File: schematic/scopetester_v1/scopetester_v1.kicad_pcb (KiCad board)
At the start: 2 copper layers, 39 parts, among them J1 CON_PWR, J2 CON_OUT, J3 AVR_ISP, J4 CON_GND, SW1 SW_Push, U1 ATmega8A-P, Y1 12MHz

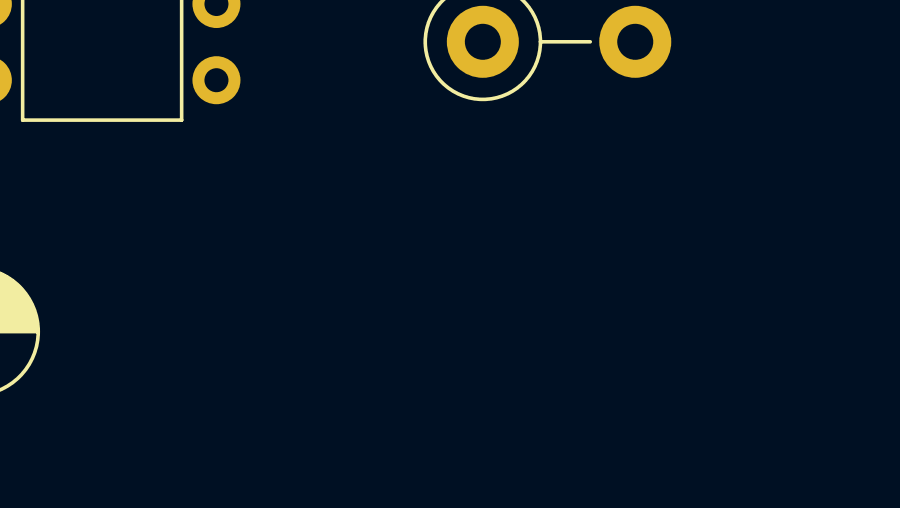
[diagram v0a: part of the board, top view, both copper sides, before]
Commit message: Replaced Vcc with +5V in schematic
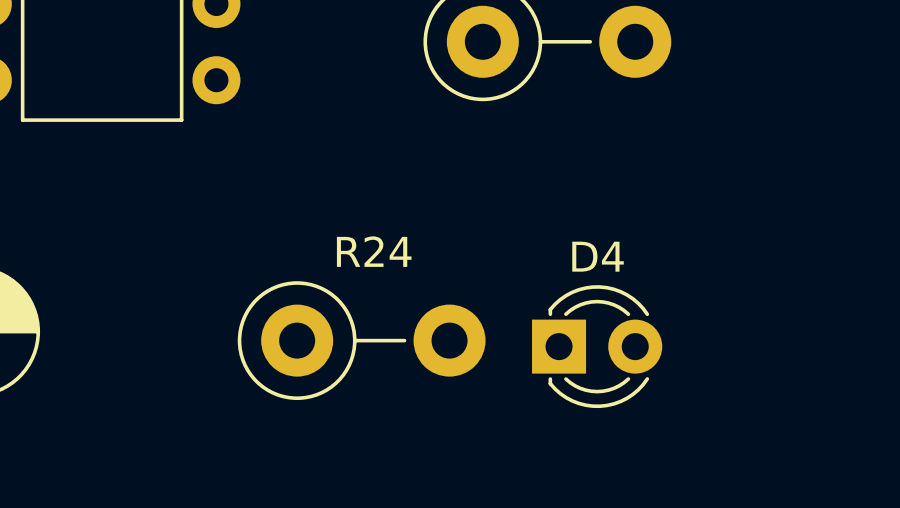
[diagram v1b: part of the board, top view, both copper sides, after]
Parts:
- added D4: LED_Small, LED_THT:LED_D3.0mm, F.Cu at (53.3, 96.5)
- added R24: 2.2k, Resistor_THT:R_Axial_DIN0411_L9.9mm_D3.6mm_P5.08mm_Vertical, F.Cu at (44.6, 96.3)
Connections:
- net VCC renamed +5V
- U1 pad 11: STAT_LED_0 -> STAT_LED_1
- U1 pad 12: STAT_LED_1 -> STAT_LED_2
- U1 pad 13: STAT_LED_2 -> STAT_LED_3
- U1 pad 6: unconnected-(U1-Pad6) -> STAT_LED_0

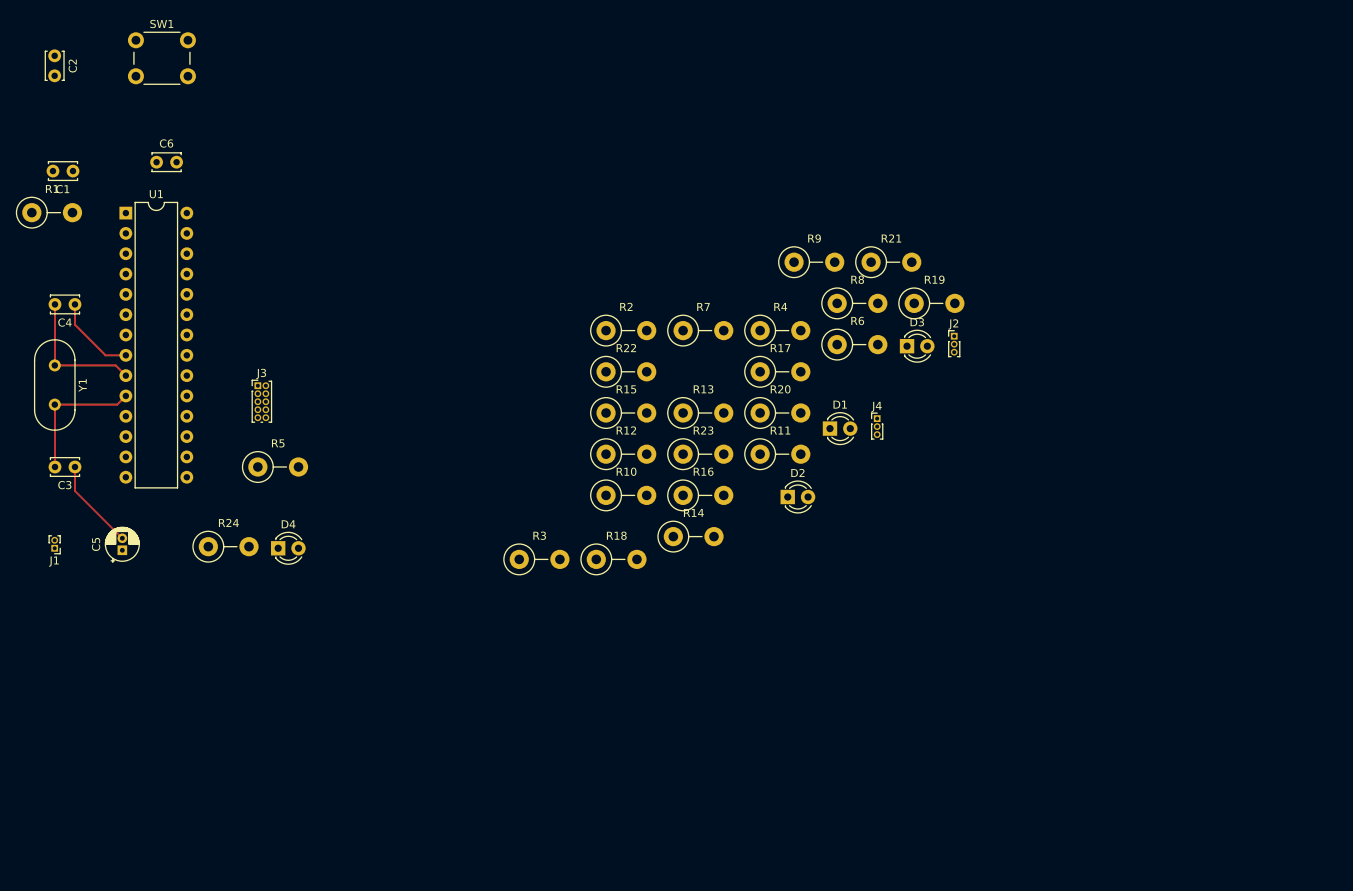
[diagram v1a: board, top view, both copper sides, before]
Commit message: Initial commit for PCB layout
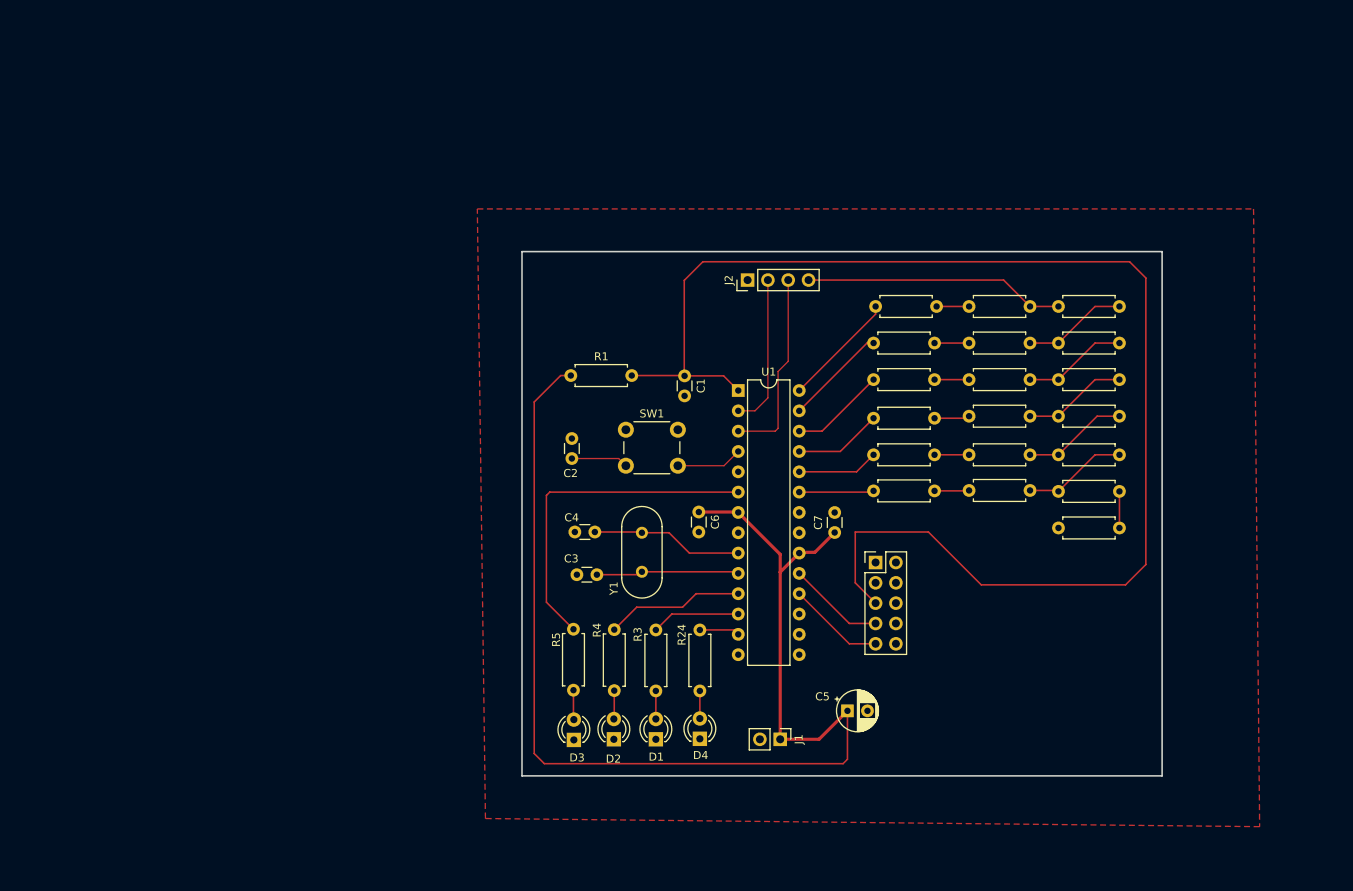
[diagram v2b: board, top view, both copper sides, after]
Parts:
- removed J4: CON_GND, Connector_PinHeader_1.00mm:PinHeader_1x03_P1.00mm_Vertical
- added C7: 100nF, Capacitor_THT:C_Disc_D3.0mm_W1.6mm_P2.50mm, F.Cu at (122.9, 94.5)
- C1, C2, C3, C4, C6: footprint Capacitor_THT:C_Disc_D3.4mm_W2.1mm_P2.50mm -> Capacitor_THT:C_Disc_D3.0mm_W1.6mm_P2.50mm
- C5: footprint Capacitor_THT:CP_Radial_D4.0mm_P1.50mm -> Capacitor_THT:CP_Radial_D5.0mm_P2.50mm
- J1: footprint Connector_PinHeader_1.00mm:PinHeader_1x02_P1.00mm_Vertical -> Connector_PinHeader_2.54mm:PinHeader_1x02_P2.54mm_Vertical
- J2: value CON_OUT -> Conn_01x04; footprint Connector_PinHeader_1.00mm:PinHeader_1x03_P1.00mm_Vertical -> Connector_PinHeader_2.54mm:PinHeader_1x04_P2.54mm_Vertical
- J3: footprint Connector_PinHeader_1.00mm:PinHeader_2x05_P1.00mm_Vertical -> Connector_PinHeader_2.54mm:PinHeader_2x05_P2.54mm_Vertical
- R1, R10, R11, R12, R13, R14, R15, R16, R17, R18, R19, R2, R20, R21, R22, R23, R24, R3, R4, R5, R6, R7, R8, R9: footprint Resistor_THT:R_Axial_DIN0411_L9.9mm_D3.6mm_P5.08mm_Vertical -> Resistor_THT:R_Axial_DIN0207_L6.3mm_D2.5mm_P7.62mm_Horizontal
- SW1: footprint Button_Switch_THT:SW_PUSH_6mm_H5mm -> Button_Switch_THT:SW_PUSH_6mm_H4.3mm
- Y1: footprint Crystal:Crystal_HC18-U_Vertical -> Crystal:Crystal_HC49-4H_Vertical
- moved J1 93.8 mm to (116.1, 120.4), turned to -90 degrees
- moved C5 92.8 mm to (124.5, 116.8), turned to 0 degrees
- moved C6 80.7 mm to (105.9, 92.0), turned to -90 degrees
- moved C1 80.6 mm to (104.1, 75.0), turned to -90 degrees
- moved C2 80.4 mm to (90.0, 82.8)
- moved J3 80.3 mm to (128.0, 98.3)
- moved U1 79.7 mm to (110.8, 76.8)
- moved SW1 78.2 mm to (96.8, 81.7)
- moved Y1 76.3 mm to (98.8, 94.6)
- moved R18 70.8 mm to (158.5, 70.9), turned to 180 degrees
- moved R1 70.4 mm to (89.9, 74.9)
- moved C4 68.7 mm to (90.4, 94.5), turned to 0 degrees
- moved D3 64.5 mm to (90.3, 120.5), turned to 90 degrees
- moved C3 64.2 mm to (90.7, 99.8), turned to 0 degrees
- moved R24 64.0 mm to (106.0, 114.3), turned to 90 degrees
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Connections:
- J2 pad 1: ANG_OUT_0 -> GND
- J2 pad 2: DIGI_OUT_1 -> DIGI_OUT_0
- J2 pad 3: DIGI_OUT_0 -> DIGI_OUT_1
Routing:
- net U1_RESET: track 0.00 -> 171.4 mm
- net +5V: track 0.00 -> 150.2 mm
- net STAT_LED_0: track 0.00 -> 42.3 mm
- net ANG_OUT_0: track 0.00 -> 32.6 mm
- net DIGI_OUT_1: track 0.00 -> 24.2 mm
- net GND: track 21.8 -> 0.00 mm
- net DIGI_OUT_0: track 0.00 -> 19.1 mm
- net STAT_LED_1: track 0.00 -> 17.4 mm
- net SW_MODE: track 0.00 -> 15.4 mm
- net ANG_D5: track 0.00 -> 14.5 mm
- net Net-(R15-Pad2): track 0.00 -> 13.2 mm
- net Net-(R16-Pad2): track 0.00 -> 13.1 mm
- net Net-(R14-Pad2): track 0.00 -> 13.1 mm
- net Net-(R13-Pad2): track 0.00 -> 13.1 mm
- net Net-(R12-Pad2): track 0.00 -> 13.1 mm
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- added copper zone on F.Cu, net GND
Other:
- board outline added: 80 x 65.5 mm
- copper layers 2 -> 4

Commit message: Multiple fixes to PCB layout (not final)
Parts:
- added JP1: Jumper_2_Bridged, Resistor_THT:R_Axial_DIN0207_L6.3mm_D2.5mm_P7.62mm_Horizontal, F.Cu at (138.4, 116.3)
- moved J1 45.9 mm to (88.4, 83.8), turned to 0 degrees
- moved C5 43.4 mm to (96.3, 83.9), turned to -90 degrees
- moved D4 21.5 mm to (90.6, 105.4), turned to 0 degrees
- moved C2 17.1 mm to (105.9, 76.5)
- moved D1 14.1 mm to (90.6, 110.4), turned to 0 degrees
- moved R24 13.1 mm to (96.6, 105.4), turned to 0 degrees
- moved R5 9.36 mm to (96.9, 120.9), turned to 0 degrees
- moved C6 8.17 mm to (106.2, 83.8)
- moved SW1 7.40 mm to (95.3, 74.5)
- moved C1 6.71 mm to (102.1, 68.6), turned to 90 degrees
- moved D2 6.67 mm to (90.5, 115.7), turned to 0 degrees
- moved R1 6.43 mm to (88.9, 68.6)
- moved R3 5.53 mm to (96.6, 110.4), turned to 0 degrees
- moved U1 5.43 mm to (111.3, 71.4)
- moved J3 4.33 mm to (130.8, 95.0)
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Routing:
- net U1_RESET: track 171.4 -> 58.7 mm
- net ISP_MOSI: track 0.00 -> 30.3 mm
- net +5V: track 150.2 -> 128.8 mm
- net STAT_LED_1: track 17.4 -> 29.0 mm
- net STAT_LED_0: track 42.3 -> 52.5 mm
- net STAT_LED_2: track 11.1 -> 20.2 mm
- net DIGI_OUT_1: track 24.2 -> 17.5 mm
- net DIGI_OUT_0: track 19.1 -> 14.0 mm
- net STAT_LED_3: track 5.03 -> 8.51 mm
- net ISP_MISO: track 12.1 -> 15.4 mm
- net ISP_SCK: track 12.1 -> 15.4 mm
- net ANG_D0: track 9.36 -> 11.7 mm
- net ANG_OUT_0: track 32.6 -> 34.5 mm
- net ANG_D1: track 10.2 -> 11.8 mm
- net Net-(C3-Pad2): track 17.9 -> 19.3 mm
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- added copper zone on B.Cu, net GND
- removed copper zone on F.Cu, net GND
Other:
- board size 80 x 65.5 mm -> 80 x 65 mm
- copper layers 4 -> 2

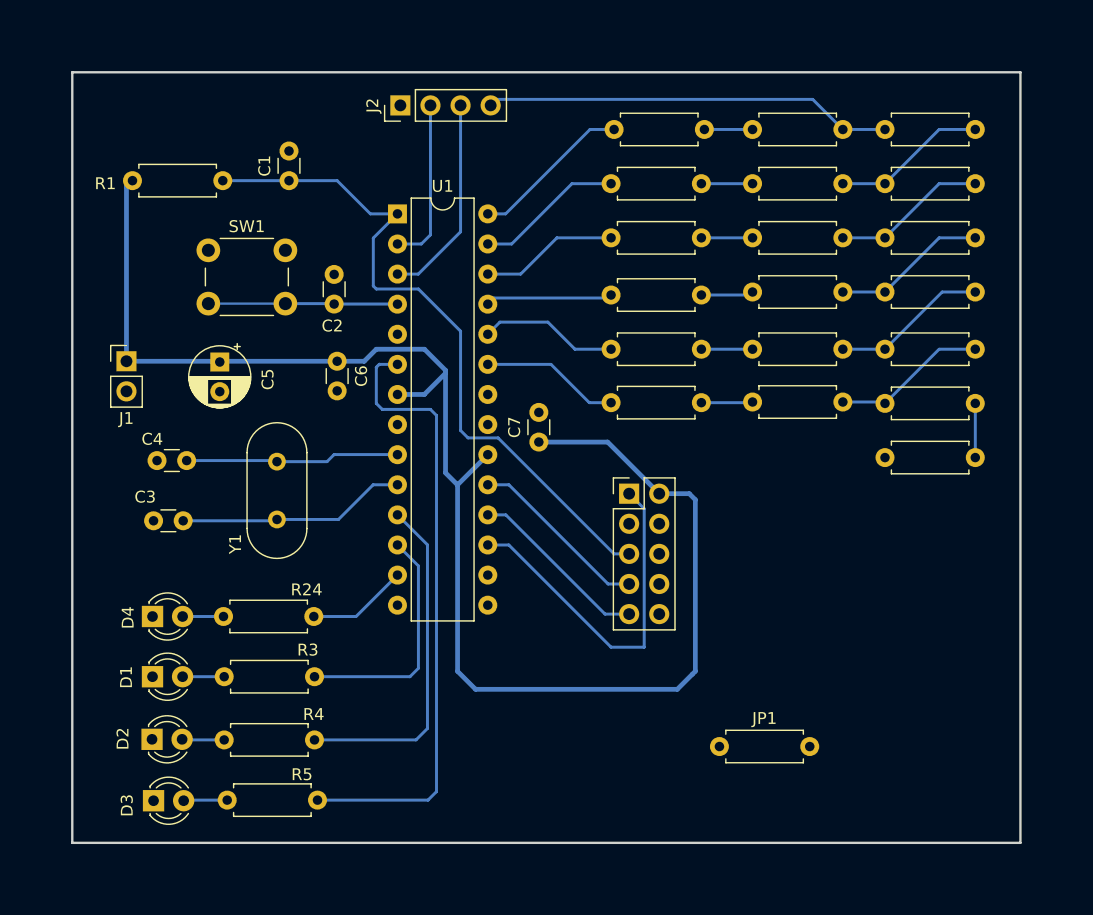
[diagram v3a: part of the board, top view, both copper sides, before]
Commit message: More compact PCB layout
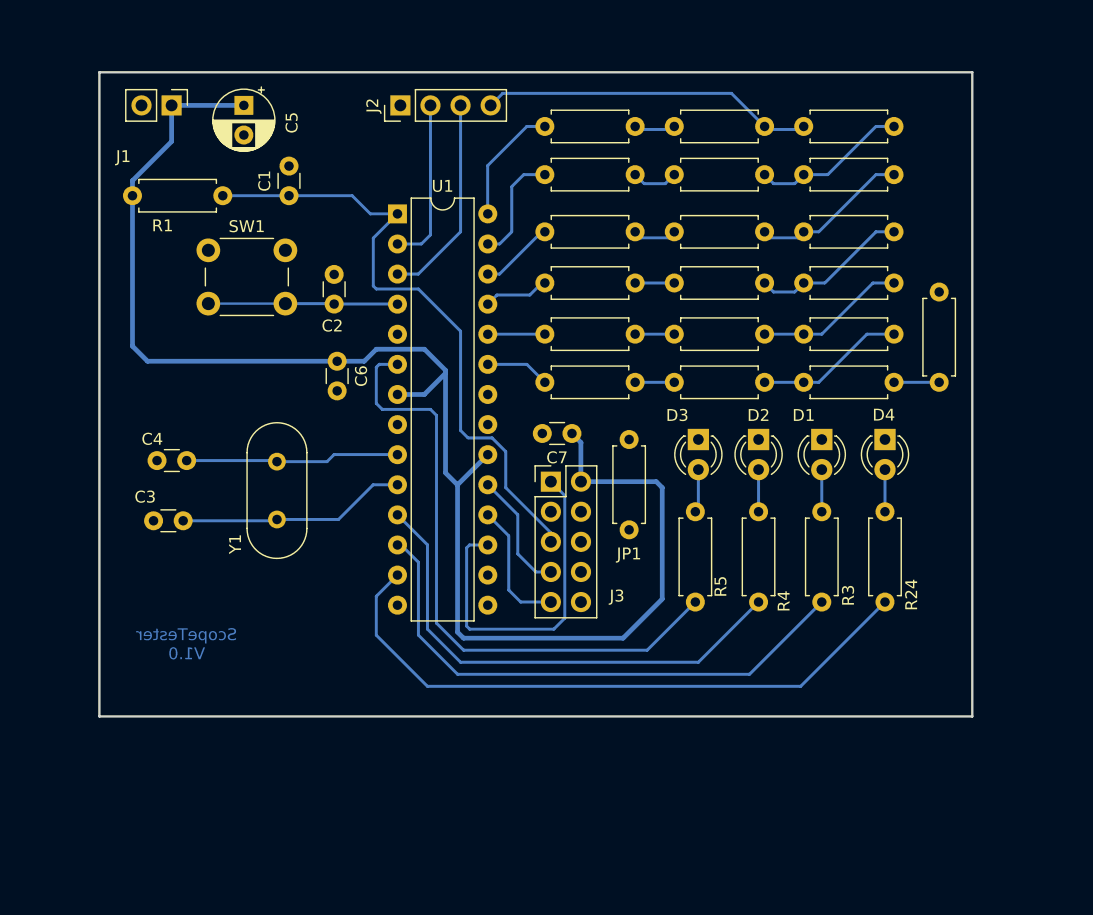
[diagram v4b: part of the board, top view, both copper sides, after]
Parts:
- moved D4 63.6 mm to (152.4, 90.4), turned to -90 degrees
- moved D1 59.9 mm to (147.1, 90.4), turned to -90 degrees
- moved D2 57.1 mm to (141.7, 90.4), turned to -90 degrees
- moved R24 56.5 mm to (152.4, 96.5), turned to -90 degrees
- moved D3 55.2 mm to (136.7, 90.4), turned to -90 degrees
- moved R3 52.3 mm to (147.1, 96.5), turned to -90 degrees
- moved R4 49.0 mm to (141.7, 96.5), turned to -90 degrees
- moved R5 46.4 mm to (136.4, 96.5), turned to -90 degrees
- moved J1 21.9 mm to (92.2, 62.2), turned to -90 degrees
- moved C5 21.8 mm to (98.3, 62.2)
- moved JP1 19.8 mm to (130.8, 98.0), turned to 90 degrees
- moved R22 7.08 mm to (145.5, 85.6)
- moved R23 7.04 mm to (157.0, 85.6), turned to 90 degrees
- moved R21 6.97 mm to (153.2, 81.5)
- moved R18 6.90 mm to (153.2, 68.1)
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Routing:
- net STAT_LED_3: track 8.51 -> 53.5 mm
- net STAT_LED_2: track 20.2 -> 46.5 mm
- net STAT_LED_1: track 29.0 -> 41.9 mm
- net ANG_D1: track 11.8 -> 4.82 mm
- net ANG_OUT_0: track 34.5 -> 28.2 mm
- net ANG_D0: track 11.7 -> 5.44 mm
- net ANG_D3: track 11.7 -> 6.29 mm
- net U1_RESET: track 58.7 -> 53.4 mm
- net ANG_D2: track 10.7 -> 5.56 mm
- net ISP_SCK: track 15.4 -> 10.3 mm
- net ISP_MISO: track 15.4 -> 11.0 mm
- net ANG_D5: track 13.6 -> 10.3 mm
- net ANG_D4: track 12.5 -> 9.47 mm
- net +5V: track 128.8 -> 126.5 mm
- net Net-(R14-Pad1): track 4.42 -> 3.30 mm
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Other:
- board size 80 x 65 mm -> 73.7 x 54.4 mm
- board text added: "ScopeTester V1.0"
